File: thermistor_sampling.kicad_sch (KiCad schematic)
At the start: 14 parts, among them Q1 BSS84, U7 74LV4051A, U8 74LV4051A, U9 74LV4051A

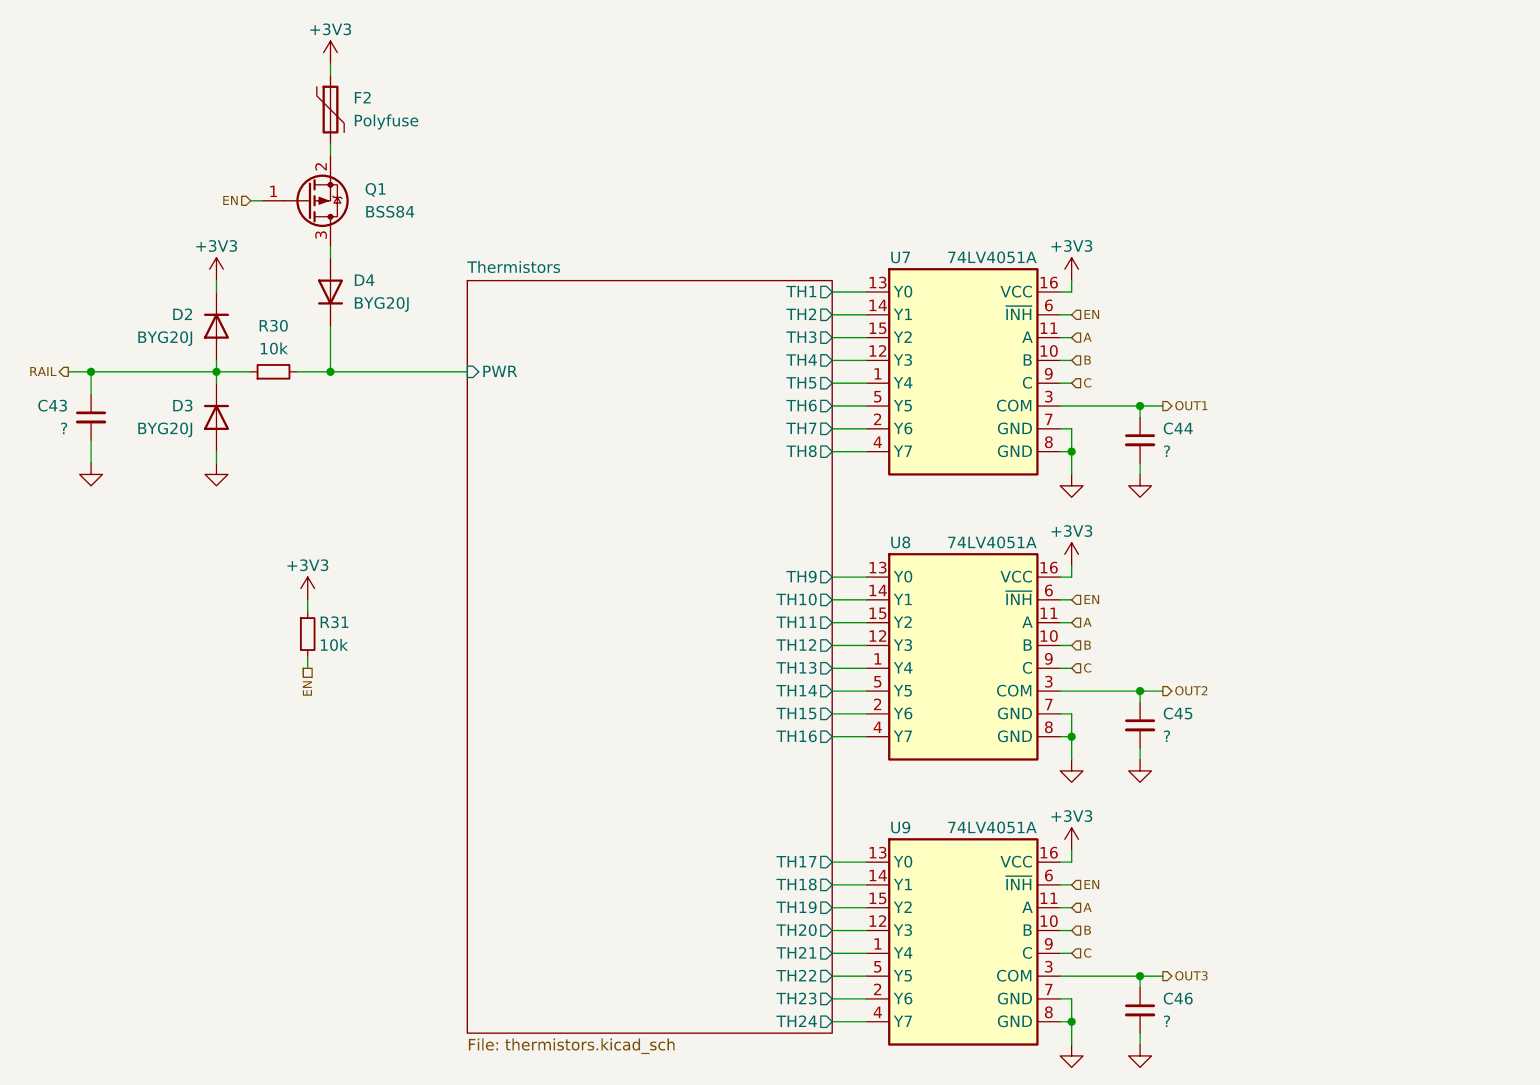
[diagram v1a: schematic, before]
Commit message: schematic: Fix-up reference designators
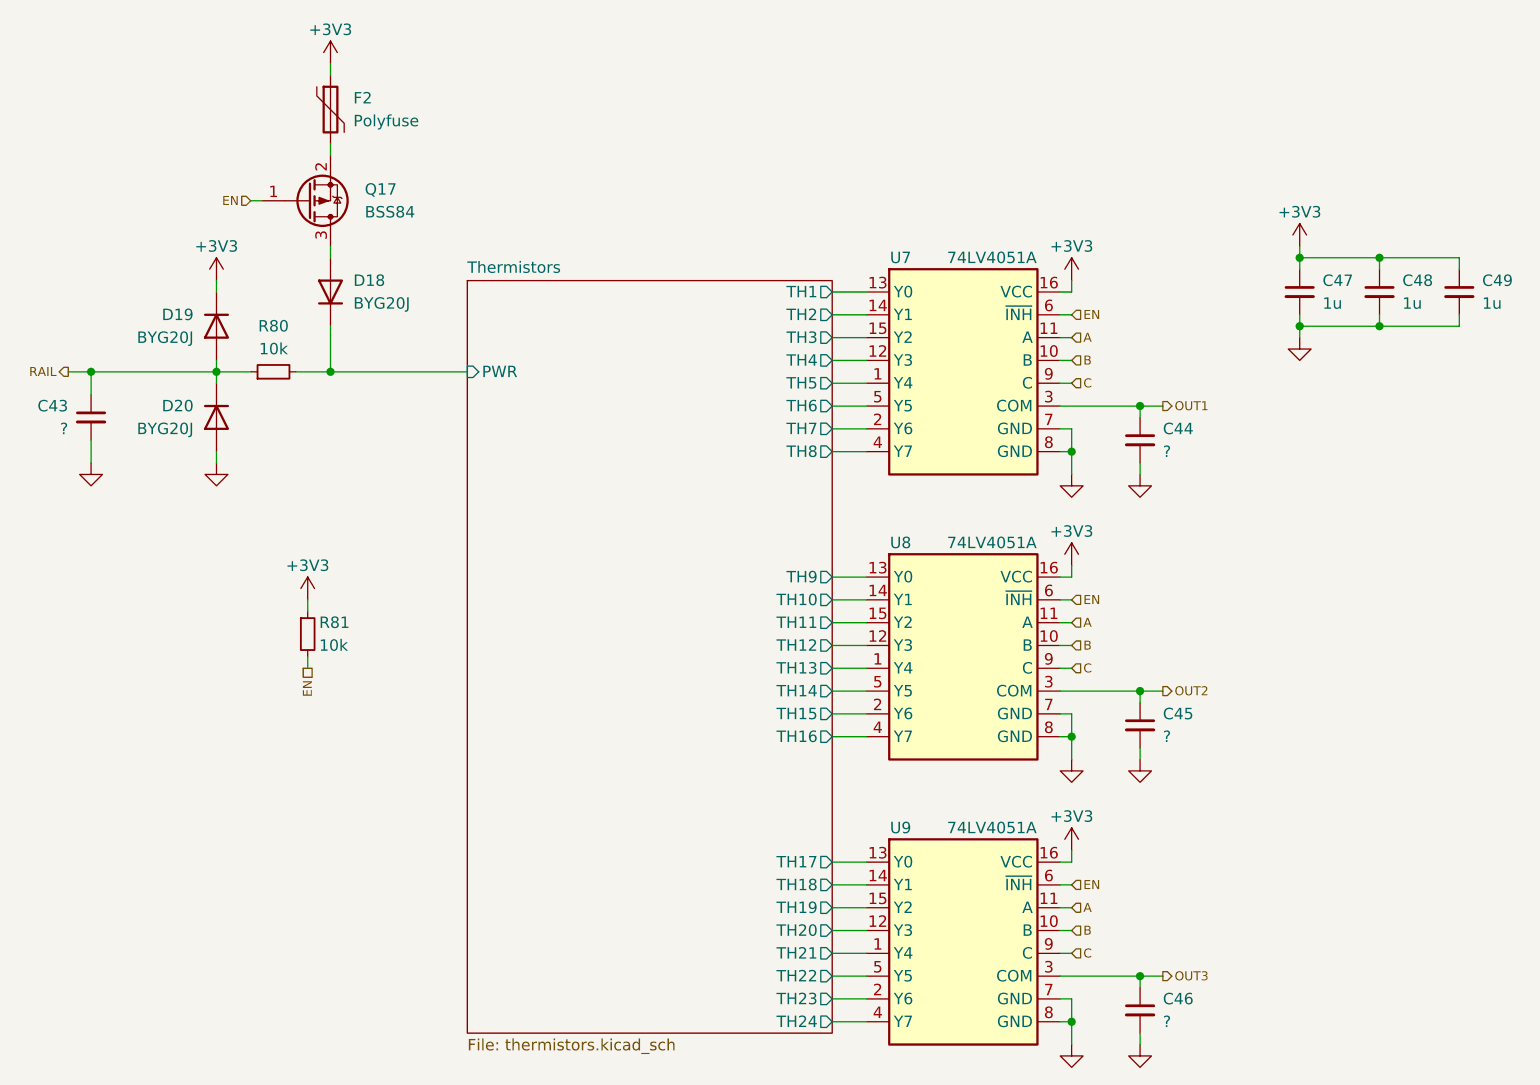
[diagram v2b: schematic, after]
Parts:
- added C47, C48, C49: 1u, Capacitor_SMD:C_0603_1608Metric, symbol Device:C_Small
- F2: Dist (none) -> LCSC; Dist # (none) -> C2153714; Mfr (none) -> Littelfuse; Mfr # (none) -> 1206L010/60WR
- renumbered D4 to D18, D2 to D19, D3 to D20, Q1 to Q17, R30 to R80, R31 to R81
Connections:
- net +3V3: now also C47.1, C48.1, C49.1
- net GND: now also C47.2, C48.2, C49.2

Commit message: Revision E
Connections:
- net Thermistors/TH1: now also U7.15 (Y2); no longer U7.13 (Y0)
- net Thermistors/TH10: now also U8.5 (Y5); no longer U8.14 (Y1)
- net Thermistors/TH12: now also U8.1 (Y4); no longer U8.12 (Y3)
- net Thermistors/TH13: now also U8.12 (Y3); no longer U8.1 (Y4)
- net Thermistors/TH14: now also U8.13 (Y0); no longer U8.5 (Y5)
- net Thermistors/TH16: now also U8.14 (Y1); no longer U8.4 (Y7)
- net Thermistors/TH17: now also U9.5 (Y5); no longer U9.13 (Y0)
- net Thermistors/TH18: now also U9.4 (Y7); no longer U9.14 (Y1)
- net Thermistors/TH19: now also U9.1 (Y4); no longer U9.15 (Y2)
- net Thermistors/TH20: now also U9.2 (Y6); no longer U9.12 (Y3)
- net Thermistors/TH21: now also U9.12 (Y3); no longer U9.1 (Y4)
- net Thermistors/TH22: now also U9.13 (Y0); no longer U9.5 (Y5)
- net Thermistors/TH23: now also U9.14 (Y1); no longer U9.2 (Y6)
- net Thermistors/TH24: now also U9.15 (Y2); no longer U9.4 (Y7)
- net Thermistors/TH3: now also U7.13 (Y0); no longer U7.15 (Y2)
- net Thermistors/TH5: now also U7.4 (Y7); no longer U7.1 (Y4)
- net Thermistors/TH7: now also U7.1 (Y4); no longer U7.2 (Y6)
- net Thermistors/TH8: now also U7.2 (Y6); no longer U7.4 (Y7)
- net Thermistors/TH9: now also U8.4 (Y7); no longer U8.13 (Y0)
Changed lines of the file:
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@@
 		)
 		(pin "TH1" output
-			(at 135.89 57.15 0)
+			(at 135.89 62.23 0)
 			(effects
 				(font
@@
 		)
 		(pin "TH3" output
-			(at 135.89 62.23 0)
+			(at 135.89 57.15 0)
 			(effects
 				(font
@@
 		)
 		(pin "TH5" output
-			(at 135.89 67.31 0)
+			(at 135.89 74.93 0)
 			(effects
 				(font
@@
 		)
 		(pin "TH7" output
+			(at 135.89 67.31 0)
+			(effects
+				(font
+					(size 1.27 1.27)
+				)
+				(justify right)
+			)
+		)
+		(pin "TH8" output
 			(at 135.89 72.39 0)
 			(effects
@@
 			)
 		)
-		(pin "TH8" output
-			(at 135.89 74.93 0)
-			(effects
-				(font
-					(size 1.27 1.27)
-				)
-				(justify right)
-			)
-		)
 		(pin "TH9" output
-			(at 135.89 88.9 0)
+			(at 135.89 106.68 0)
 			(effects
 				(font
@@
 		)
 		(pin "TH10" output
-			(at 135.89 91.44 0)
+			(at 135.89 101.6 0)
 			(effects
 				(font
@@
 		)
 		(pin "TH12" output
+			(at 135.89 99.06 0)
+			(effects
+				(font
+					(size 1.27 1.27)
+				)
+				(justify right)
+			)
+		)
+		(pin "TH13" output
 			(at 135.89 96.52 0)
 			(effects
@@
 			)
 		)
-		(pin "TH13" output
-			(at 135.89 99.06 0)
-			(effects
-				(font
-					(size 1.27 1.27)
-				)
-				(justify right)
-			)
-		)
 		(pin "TH14" output
-			(at 135.89 101.6 0)
+			(at 135.89 88.9 0)
 			(effects
 				(font
@@
 		)
 		(pin "TH16" output
-			(at 135.89 106.68 0)
+			(at 135.89 91.44 0)
 			(effects
 				(font
@@
 		)
 		(pin "TH17" output
+			(at 135.89 133.35 0)
+			(effects
+				(font
+					(size 1.27 1.27)
+				)
+				(justify right)
+			)
+		)
+		(pin "TH18" output
+			(at 135.89 138.43 0)
+			(effects
+				(font
+					(size 1.27 1.27)
+				)
+				(justify right)
+			)
+		)
+		(pin "TH19" output
+			(at 135.89 130.81 0)
+			(effects
+				(font
+					(size 1.27 1.27)
+				)
+				(justify right)
+			)
+		)
+		(pin "TH20" output
+			(at 135.89 135.89 0)
+			(effects
+				(font
+					(size 1.27 1.27)
+				)
+				(justify right)
+			)
+		)
+		(pin "TH21" output
+			(at 135.89 128.27 0)
+			(effects
+				(font
+					(size 1.27 1.27)
+				)
+				(justify right)
+			)
+		)
+		(pin "TH22" output
 			(at 135.89 120.65 0)
 			(effects
@@
 			)
 		)
-		(pin "TH18" output
+		(pin "TH23" output
 			(at 135.89 123.19 0)
 			(effects
@@
 			)
 		)
-		(pin "TH19" output
+		(pin "TH24" output
 			(at 135.89 125.73 0)
 			(effects
 				(font
-					(size 1.27 1.27)
-				)
-				(justify right)
-			)
-		)
-		(pin "TH20" output
-			(at 135.89 128.27 0)
-			(effects
-				(font
-					(size 1.27 1.27)
-				)
-				(justify right)
-			)
-		)
-		(pin "TH21" output
-			(at 135.89 130.81 0)
-			(effects
-				(font
-					(size 1.27 1.27)
-				)
-				(justify right)
-			)
-		)
-		(pin "TH22" output
-			(at 135.89 133.35 0)
-			(effects
-				(font
-					(size 1.27 1.27)
-				)
-				(justify right)
-			)
-		)
-		(pin "TH23" output
-			(at 135.89 135.89 0)
-			(effects
-				(font
-					(size 1.27 1.27)
-				)
-				(justify right)
-			)
-		)
-		(pin "TH24" output
-			(at 135.89 138.43 0)
-			(effects
-				(font

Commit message: *: Minor cleanup
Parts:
- C43, C44, C45, C46: value ? -> 1u; Dist (none) -> LCSC; Dist # (none) -> C5199872; Mfr (none) -> Samsung; Mfr # (none) -> CL10B105KB8NQNC
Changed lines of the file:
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@@
 			)
 		)
-		(property "Value" "?"
+		(property "Value" "1u"
 			(at 172.72 106.6862 0)
 			(effects
@@
 		)
 		(property "Description" "Unpolarized capacitor, small symbol"
+			(at 170.18 105.41 0)
+			(effects
+				(font
+					(size 1.27 1.27)
+				)
+				(hide yes)
+			)
+		)
+		(property "Dist" "LCSC"
+			(at 170.18 105.41 0)
+			(effects
+				(font
+					(size 1.27 1.27)
+				)
+				(hide yes)
+			)
+		)
+		(property "Dist #" "C5199872"
+			(at 170.18 105.41 0)
+			(effects
+				(font
+					(size 1.27 1.27)
+				)
+				(hide yes)
+			)
+		)
+		(property "Mfr" "Samsung"
+			(at 170.18 105.41 0)
+			(effects
+				(font
+					(size 1.27 1.27)
+				)
+				(hide yes)
+			)
+		)
+		(property "Mfr #" "CL10B105KB8NQNC"
 			(at 170.18 105.41 0)
 			(effects
@@
 			)
 		)
-		(property "Value" "?"
+		(property "Value" "1u"
 			(at 172.72 138.4362 0)
 			(effects
@@
 		)
 		(property "Description" "Unpolarized capacitor, small symbol"
+			(at 170.18 137.16 0)
+			(effects
+				(font
+					(size 1.27 1.27)
+				)
+				(hide yes)
+			)
+		)
+		(property "Dist" "LCSC"
+			(at 170.18 137.16 0)
+			(effects
+				(font
+					(size 1.27 1.27)
+				)
+				(hide yes)
+			)
+		)
+		(property "Dist #" "C5199872"
+			(at 170.18 137.16 0)
+			(effects
+				(font
+					(size 1.27 1.27)
+				)
+				(hide yes)
+			)
+		)
+		(property "Mfr" "Samsung"
+			(at 170.18 137.16 0)
+			(effects
+				(font
+					(size 1.27 1.27)
+				)
+				(hide yes)
+			)
+		)
+		(property "Mfr #" "CL10B105KB8NQNC"
 			(at 170.18 137.16 0)
 			(effects
@@
 			)
 		)
-		(property "Value" "?"
+		(property "Value" "1u"
 			(at 50.8 72.3962 0)
 			(effects
@@
 		)
 		(property "Description" "Unpolarized capacitor, small symbol"
+			(at 53.34 71.12 0)
+			(effects
+				(font
+					(size 1.27 1.27)
+				)
+				(hide yes)
+			)
+		)
+		(property "Dist" "LCSC"
+			(at 53.34 71.12 0)
+			(effects
+				(font
+					(size 1.27 1.27)
+				)
+				(hide yes)
+			)
+		)
+		(property "Dist #" "C5199872"
+			(at 53.34 71.12 0)
+			(effects
+				(font
+					(size 1.27 1.27)
+				)
+				(hide yes)
+			)
+		)
+		(property "Mfr" "Samsung"
+			(at 53.34 71.12 0)
+			(effects
+				(font
+					(size 1.27 1.27)
+				)
+				(hide yes)
+			)
+		)
+		(property "Mfr #" "CL10B105KB8NQNC"
 			(at 53.34 71.12 0)
 			(effects
@@
 			)
 		)
-		(property "Value" "?"
+		(property "Value" "1u"
 			(at 172.72 74.9362 0)
 			(effects
@@
 			(at 170.18 73.66 0)
 			(effects
+				(font
+					(size 1.27 1.27)
+				)
+				(hide yes)
+			)
+		)
+		(property "Dist" "LCSC"
+			(at 170.18 73.66 0)
+			(effects
+				(font
+					(size 1.27 1.27)
+				)
+				(hide yes)
+			)
+		)
+		(property "Dist #" "C5199872"
+			(at 170.18 73.66 0)
+			(effects
+				(font
+					(size 1.27 1.27)
+				)
+				(hide yes)
+			)
+		)
+		(property "Mfr" "Samsung"
+			(at 170.18 73.66 0)
+			(effects
+				(font
+					(size 1.27 1.27)
+				)
+				(hide yes)
+			)
+		)
+		(property "Mfr #" "CL10B105KB8NQNC"
+			(at 170.18 73.66 0)
+			(effects

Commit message: *: Rework BOM
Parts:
- C43, C44, C45, C46, C47, C48, C49: Dist LCSC -> (none); Dist # C5199872 -> (none); LCSC # (none) -> C5199872; Mouser # (none) -> 187-CL10B105KB8NQNC
- D18, D19, D20: DigiKey # (none) -> BYG20J-E3/TR3GICT-ND; LCSC # (none) -> C241925; Mfr (none) -> Vishay; Mfr # (none) -> BYG20J-E3/TR; Mouser # (none) -> 625-BYG20J-E3/TR3
- F2: DigiKey # (none) -> F8129CT-ND; Dist LCSC -> (none); Dist # C2153714 -> (none); LCSC # (none) -> C315892; Mfr # 1206L010/60WR -> 1206L005/60WR; Mouser # (none) -> 576-1206L005/60WR
- Q17: DigiKey # (none) -> BSS84LT1GOSCT-ND; LCSC # (none) -> C82079; Mfr (none) -> onsemi; Mfr # (none) -> BSS84LT1G; Mouser # (none) -> 863-BSS84LT1G
- R80, R81: LCSC # (none) -> C25804; Mfr (none) -> Uni-Royal; Mfr # (none) -> 0603WAF1002T5E
- U7, U8, U9: DigiKey # (none) -> 296-3829-1-ND; LCSC # (none) -> C7793; Mfr (none) -> Texas Instruments; Mfr # (none) -> SN74LV4051APWR; Mouser # (none) -> 595-SN74LV4051APWR

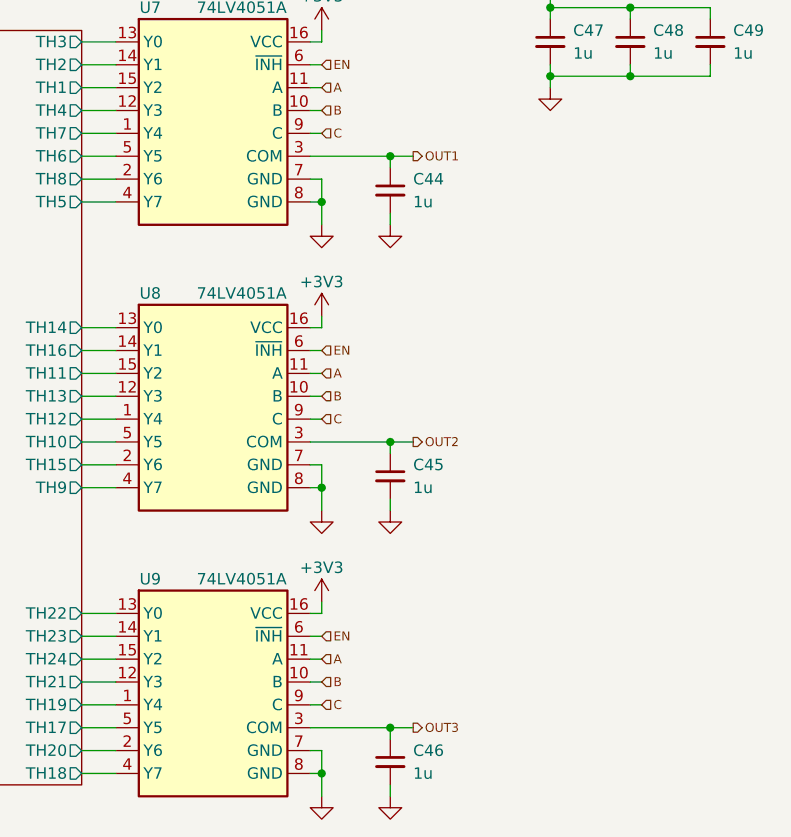
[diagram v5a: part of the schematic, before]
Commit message: schematic: Lower MUX output filter capacitance and mark DNP
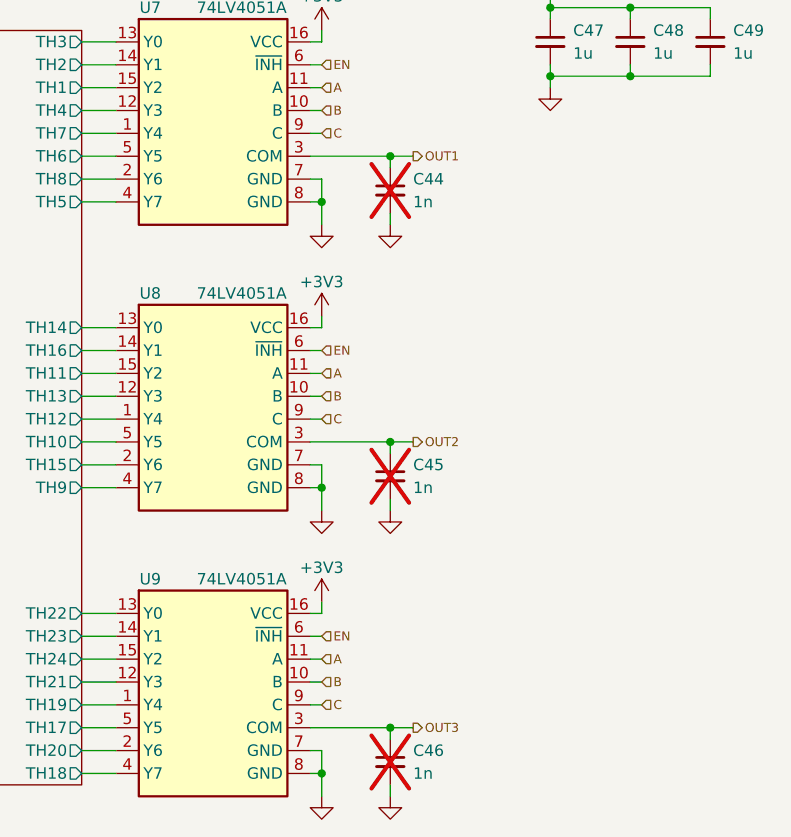
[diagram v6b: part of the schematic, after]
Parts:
- C44, C45, C46: value 1u -> 1n; LCSC # C5199872 -> (none); Mfr Samsung -> (none); Mfr # CL10B105KB8NQNC -> (none); Mouser # 187-CL10B105KB8NQNC -> (none); now not fitted
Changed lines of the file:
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@@
 		(in_bom yes)
 		(on_board yes)
-		(dnp no)
+		(dnp yes)
 		(fields_autoplaced yes)
 		(property "Reference" "C45"
@@
 			)
 		)
-		(property "Value" "1u"
+		(property "Value" "1n"
 			(at 172.72 106.6862 0)
 			(effects
@@
 			)
 		)
-		(property "Mfr" "Samsung"
+		(property "Mfr" ""
 			(at 170.18 105.41 0)
 			(effects
@@
 			)
 		)
-		(property "Mfr #" "CL10B105KB8NQNC"
+		(property "Mfr #" ""
 			(at 170.18 105.41 0)
 			(effects
@@
 			)
 		)
-		(property "LCSC #" "C5199872"
+		(property "LCSC #" ""
 			(at 170.18 105.41 0)
 			(effects
@@
 			)
 		)
-		(property "Mouser #" "187-CL10B105KB8NQNC"
+		(property "Mouser #" ""
 			(at 170.18 105.41 0)
 			(effects
@@
 		(in_bom yes)
 		(on_board yes)
-		(dnp no)
+		(dnp yes)
 		(fields_autoplaced yes)
 		(property "Reference" "C46"
@@
 			)
 		)
-		(property "Value" "1u"
+		(property "Value" "1n"
 			(at 172.72 138.4362 0)
 			(effects
@@
 			)
 		)
-		(property "Mfr" "Samsung"
+		(property "Mfr" ""
 			(at 170.18 137.16 0)
 			(effects
@@
 			)
 		)
-		(property "Mfr #" "CL10B105KB8NQNC"
+		(property "Mfr #" ""
 			(at 170.18 137.16 0)
 			(effects
@@
 			)
 		)
-		(property "LCSC #" "C5199872"
+		(property "LCSC #" ""
 			(at 170.18 137.16 0)
 			(effects
@@
 			)
 		)
-		(property "Mouser #" "187-CL10B105KB8NQNC"
+		(property "Mouser #" ""
 			(at 170.18 137.16 0)
 			(effects
@@
 		(in_bom yes)
 		(on_board yes)
-		(dnp no)
+		(dnp yes)
 		(fields_autoplaced yes)
 		(property "Reference" "C44"
@@
 			)
 		)
-		(property "Value" "1u"
+		(property "Value" "1n"
 			(at 172.72 74.9362 0)
 			(effects
@@
 			)
 		)
-		(property "Mfr" "Samsung"
+		(property "Mfr" ""
 			(at 170.18 73.66 0)
 			(effects
@@
 			)
 		)
-		(property "Mfr #" "CL10B105KB8NQNC"
+		(property "Mfr #" ""
 			(at 170.18 73.66 0)
 			(effects
@@
 			)
 		)
-		(property "LCSC #" "C5199872"
+		(property "LCSC #" ""
 			(at 170.18 73.66 0)
 			(effects
@@
 			)
 		)
-		(property "Mouser #" "187-CL10B105KB8NQNC"
+		(property "Mouser #" ""
 			(at 170.18 73.66 0)
 			(effects
